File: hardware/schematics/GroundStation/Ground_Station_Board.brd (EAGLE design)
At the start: 50.5 x 66 mm, 11 parts

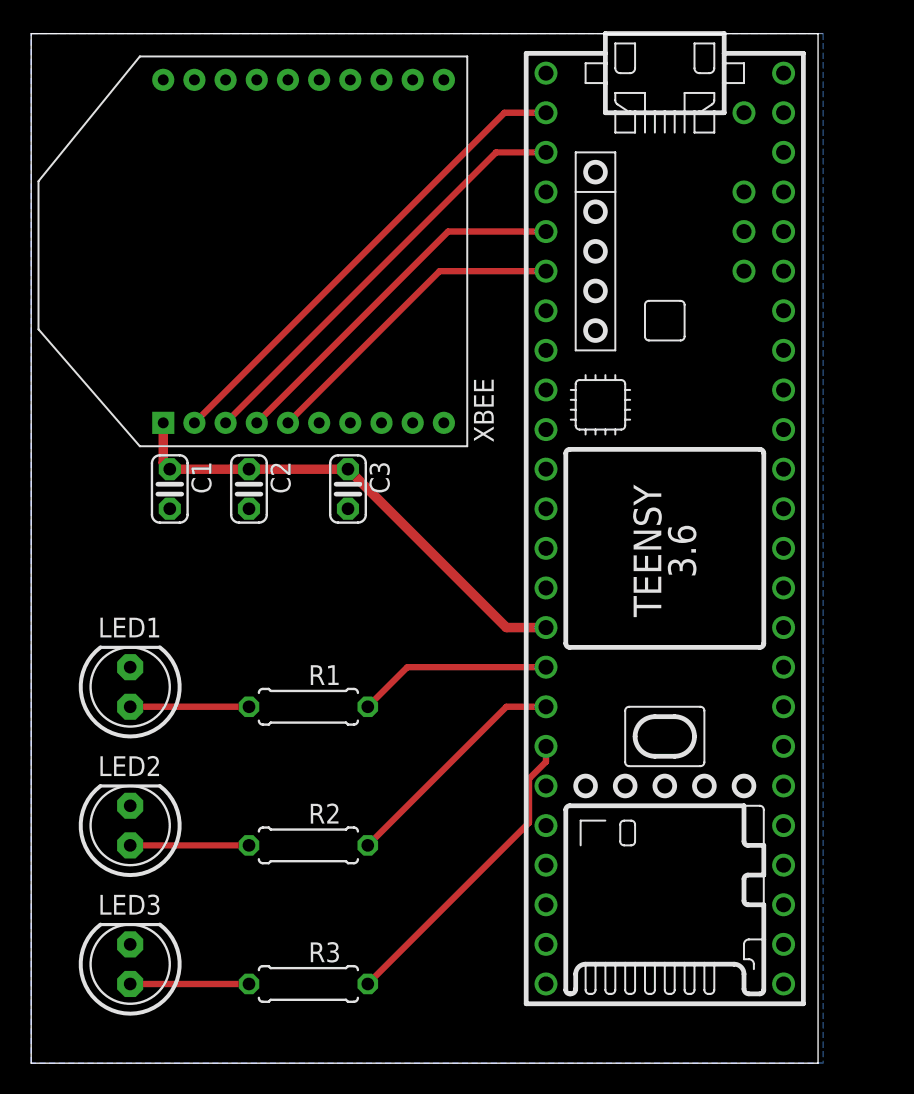
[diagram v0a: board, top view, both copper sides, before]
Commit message: Changed Xbee -> Xbee-Pro | Added render png
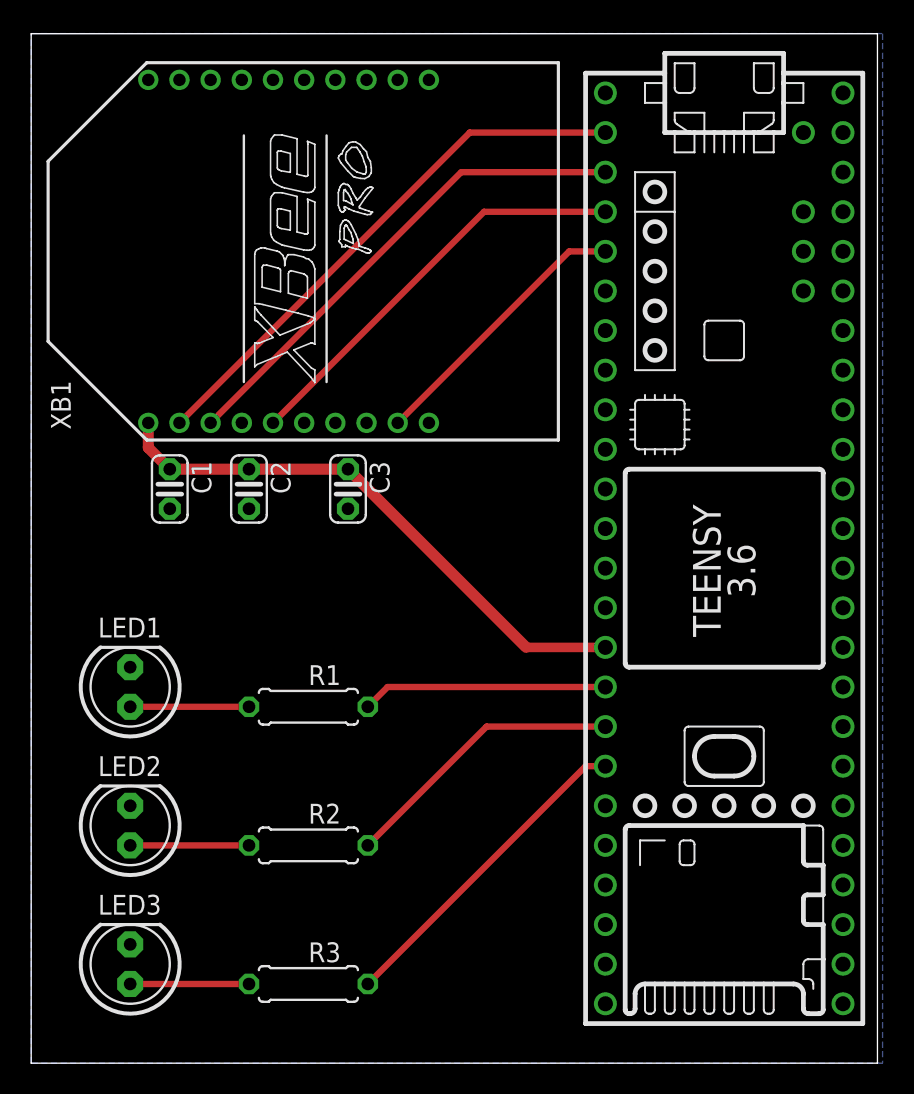
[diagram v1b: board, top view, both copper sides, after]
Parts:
- removed XBEE: XBEE, adafruit:XBEE
- added XB1: XBEE-PRO, xbee:XBEE-PRO
- moved U$2 4.02 mm to (44.5, 48.3)
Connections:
- net +3V3: now also XB1.1; no longer XBEE.1
- net GND: now also XB1.10, XB1.14; no longer XBEE.10, XBEE.14
- net XBEE_EN: now also XB1.9; no longer XBEE.4
- net XBEE_RST: now also U$2.2, XB1.5; no longer U$2.4/CANRX, XBEE.5
- net XBEE_RX: now also XB1.3; no longer XBEE.3
- net XBEE_TX: now also XB1.2; no longer XBEE.2
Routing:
- net XBEE_RST: track 20.6 -> 26.9 mm
- net XBEE_EN: track 23.6 -> 17.9 mm
- net +3V3: track 31.5 -> 36.8 mm
- net XBEE_RX: track 27.7 -> 32.0 mm
- net XBEE_TX: track 30.8 -> 35.0 mm
- net LED_2: track 15.1 -> 18.4 mm
- net LED_1: track 12.5 -> 15.8 mm
- net LED_3: track 20.0 -> 21.0 mm
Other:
- board size 50.5 x 66 mm -> 54.3 x 66 mm
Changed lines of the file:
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@@
 <drawing>
 <settings>
-<setting alwaysvectorfont="no"/>
+<setting alwaysvectorfont="yes"/>
 <setting verticaltext="up"/>
 </settings>
@@
 <layers>
 <layer number="1" name="Top" color="4" fill="1" visible="yes" active="yes"/>
+<layer number="2" name="Route2" color="1" fill="3" visible="no" active="no"/>
+<layer number="3" name="Route3" color="4" fill="3" visible="no" active="no"/>
+<layer number="4" name="Route4" color="1" fill="4" visible="no" active="no"/>
+<layer number="5" name="Route5" color="4" fill="4" visible="no" active="no"/>
+<layer number="6" name="Route6" color="1" fill="8" visible="no" active="no"/>
+<layer number="7" name="Route7" color="4" fill="8" visible="no" active="no"/>
+<layer number="8" name="Route8" color="1" fill="2" visible="no" active="no"/>
+<layer number="9" name="Route9" color="4" fill="2" visible="no" active="no"/>
+<layer number="10" name="Route10" color="1" fill="7" visible="no" active="no"/>
+<layer number="11" name="Route11" color="4" fill="7" visible="no" active="no"/>
+<layer number="12" name="Route12" color="1" fill="5" visible="no" active="no"/>
+<layer number="13" name="Route13" color="4" fill="5" visible="no" active="no"/>
+<layer number="14" name="Route14" color="1" fill="6" visible="no" active="no"/>
+<layer number="15" name="Route15" color="4" fill="6" visible="no" active="no"/>
 <layer number="16" name="Bottom" color="1" fill="1" visible="yes" active="yes"/>
 <layer number="17" name="Pads" color="2" fill="1" visible="yes" active="yes"/>
@@
 <board>
 <plain>
-<wire x1="0" y1="13.97" x2="50.47" y2="13.97" width="0" layer="20"/>
-<wire x1="50.47" y1="13.97" x2="50.47" y2="80" width="0" layer="20"/>
-<wire x1="50.47" y1="80" x2="0" y2="80" width="0" layer="20"/>
+<wire x1="0" y1="13.97" x2="54.28" y2="13.97" width="0" layer="20"/>
+<wire x1="54.28" y1="13.97" x2="54.28" y2="80" width="0" layer="20"/>
+<wire x1="54.28" y1="80" x2="0" y2="80" width="0" layer="20"/>
 <wire x1="0" y1="80" x2="0" y2="13.97" width="0" layer="20"/>
 </plain>
@@
 <attribute name="VALUE" x="18.034" y="18.4912" size="1.27" layer="27" ratio="10"/>
 </element>
-<element name="XBEE" library="adafruit" library_urn="urn:adsk.eagle:library:420" package="XBEE" package3d_urn="urn:adsk.eagle:package:6240840/1" value="XBEE" x="13.97" y="66.04" smashed="yes" rot="R90">
-<attribute name="NAME" x="28.4" y="57.91" size="1.27" layer="25" rot="R270"/>
-</element>
-<element name="U$2" library="Teensy356" package="TEENSY_3.5/3.6_BASIC" value="TEENSY_3.5/3.6_BASIC" x="40.64" y="49.53" smashed="yes" rot="R270"/>
+<element name="U$2" library="Teensy356" package="TEENSY_3.5/3.6_BASIC" value="TEENSY_3.5/3.6_BASIC" x="44.45" y="48.26" smashed="yes" rot="R270"/>
+<element name="XB1" library="xbee" package="XBEE-PRO" value="XBEE-PRO" x="16.51" y="66.04" smashed="yes" rot="R90">
+<attribute name="MF" value="" x="16.51" y="66.04" size="1.778" layer="27" rot="R90" display="off"/>
+<attribute name="MPN" value="XBP24-AWI-001" x="16.51" y="66.04" size="1.778" layer="27" rot="R90" display="off"/>
+<attribute name="NAME" x="2.54" y="54.61" size="1.27" layer="25" rot="R90"/>
+<attribute name="OC_FARNELL" value="1337916" x="16.51" y="66.04" size="1.778" layer="27" rot="R90" display="off"/>
+<attribute name="OC_NEWARK" value="42M2667" x="16.51" y="66.04" size="1.778" layer="27" rot="R90" display="off"/>
+<attribute name="VALUE" x="35.81" y="54.61" size="1.27" layer="27" rot="R90"/>
+</element>
 </elements>
 <signals>
 <signal name="GND">
-<contactref element="XBEE" pad="10"/>
-<contactref element="XBEE" pad="14"/>
 <contactref element="C2" pad="2"/>
 <contactref element="C1" pad="2"/>
@@
 <polygon width="0.1524" layer="16">
 <vertex x="0" y="80.01"/>
-<vertex x="50.8" y="80.01"/>
-<vertex x="50.8" y="13.97"/>
+<vertex x="54.61" y="80.01"/>
+<vertex x="54.61" y="13.97"/>
 <vertex x="0" y="13.97"/>
 </polygon>
+<contactref element="XB1" pad="10"/>
+<contactref element="XB1" pad="14"/>
 </signal>
 <signal name="XBEE_TX">
-<contactref element="XBEE" pad="2"/>
 <contactref element="U$2" pad="0/RX"/>
-<wire x1="10.47" y1="55.04" x2="30.36" y2="74.93" width="0.4064" layer="1"/>
-<wire x1="30.36" y1="74.93" x2="33.02" y2="74.93" width="0.4064" layer="1"/>
+<contactref element="XB1" pad="2"/>
+<wire x1="9.51" y1="55.04" x2="28.13" y2="73.66" width="0.4064" layer="1"/>
+<wire x1="28.13" y1="73.66" x2="36.83" y2="73.66" width="0.4064" layer="1"/>
 </signal>
 <signal name="XBEE_RX">
-<contactref element="XBEE" pad="3"/>
 <contactref element="U$2" pad="1/TX"/>
-<wire x1="12.47" y1="55.04" x2="29.82" y2="72.39" width="0.4064" layer="1"/>
-<wire x1="29.82" y1="72.39" x2="33.02" y2="72.39" width="0.4064" layer="1"/>
+<contactref element="XB1" pad="3"/>
+<wire x1="11.51" y1="55.04" x2="27.59" y2="71.12" width="0.4064" layer="1"/>
+<wire x1="27.59" y1="71.12" x2="36.83" y2="71.12" width="0.4064" layer="1"/>
 </signal>
 <signal name="XBEE_EN">
-<contactref element="XBEE" pad="4"/>
+<contactref element="XB1" pad="9"/>
 <contactref element="U$2" pad="3/CANTX"/>
-<wire x1="14.47" y1="55.04" x2="26.74" y2="67.31" width="0.4064" layer="1"/>
-<wire x1="26.74" y1="67.31" x2="33.02" y2="67.31" width="0.4064" layer="1"/>
+<wire x1="23.51" y1="55.04" x2="34.51" y2="66.04" width="0.4064" layer="1"/>
+<wire x1="34.51" y1="66.04" x2="36.83" y2="66.04" width="0.4064" layer="1"/>
 </signal>
 <signal name="XBEE_RST">
-<contactref element="XBEE" pad="5"/>
-<contactref element="U$2" pad="4/CANRX"/>
-<wire x1="16.47" y1="55.04" x2="26.2" y2="64.77" width="0.4064" layer="1"/>
-<wire x1="26.2" y1="64.77" x2="33.02" y2="64.77" width="0.4064" layer="1"/>
+<contactref element="XB1" pad="5"/>
+<contactref element="U$2" pad="2"/>
+<wire x1="29.05" y1="68.58" x2="36.83" y2="68.58" width="0.4064" layer="1"/>
+<wire x1="15.51" y1="55.04" x2="29.05" y2="68.58" width="0.4064" layer="1"/>
 </signal>
 <signal name="V_USB">
@@
 </signal>
 <signal name="+3V3">
-<contactref element="XBEE" pad="1"/>
 <contactref element="C2" pad="1"/>
 <contactref element="C3" pad="1"/>
 <contactref element="C1" pad="1"/>
-<wire x1="8.47" y1="55.04" x2="8.47" y2="52.49" width="0.6096" layer="1"/>
 <wire x1="8.89" y1="52.07" x2="8.47" y2="52.49" width="0.6096" layer="1"/>
-<wire x1="13.97" y1="52.07" x2="8.89" y2="52.07" width="0.6096" layer="1"/>
-<wire x1="13.97" y1="52.07" x2="20.32" y2="52.07" width="0.6096" layer="1"/>
+<wire x1="13.97" y1="52.07" x2="8.89" y2="52.07" width="0.7112" layer="1"/>
+<wire x1="13.97" y1="52.07" x2="20.32" y2="52.07" width="0.7112" layer="1"/>
 <contactref element="U$2" pad="3V3"/>
-<wire x1="20.32" y1="52.07" x2="30.48" y2="41.91" width="0.6096" layer="1"/>
-<wire x1="30.48" y1="41.91" x2="33.02" y2="41.91" width="0.6096" layer="1"/>
+<wire x1="20.32" y1="52.07" x2="31.75" y2="40.64" width="0.7112" layer="1"/>
+<wire x1="31.75" y1="40.64" x2="36.83" y2="40.64" width="0.6096" layer="1"/>
+<contactref element="XB1" pad="1"/>
+<wire x1="8.89" y1="52.07" x2="7.51" y2="53.45" width="0.7112" layer="1"/>
+<wire x1="7.51" y1="53.45" x2="7.51" y2="55.04" width="0.7112" layer="1"/>
 </signal>
 <signal name="LED_1">
 <contactref element="R1" pad="2"/>
 <contactref element="U$2" pad="24"/>
-<wire x1="21.59" y1="36.83" x2="24.13" y2="39.37" width="0.4064" layer="1"/>
-<wire x1="24.13" y1="39.37" x2="33.02" y2="39.37" width="0.4064" layer="1"/>
+<wire x1="21.59" y1="36.83" x2="22.86" y2="38.1" width="0.4064" layer="1"/>
+<wire x1="22.86" y1="38.1" x2="36.83" y2="38.1" width="0.4064" layer="1"/>
 </signal>
 <signal name="LED_2">
 <contactref element="R2" pad="2"/>
 <contactref element="U$2" pad="25"/>
-<wire x1="21.59" y1="27.94" x2="30.48" y2="36.83" width="0.4064" layer="1"/>
-<wire x1="30.48" y1="36.83" x2="33.02" y2="36.83" width="0.4064" layer="1"/>
+<wire x1="21.59" y1="27.94" x2="29.21" y2="35.56" width="0.4064" layer="1"/>
+<wire x1="29.21" y1="35.56" x2="36.83" y2="35.56" width="0.4064" layer="1"/>
 </signal>
 <signal name="LED_3">
 <contactref element="R3" pad="2"/>
 <contactref element="U$2" pad="26"/>
-<wire x1="21.59" y1="19.05" x2="31.9278" y2="29.3878" width="0.4064" layer="1"/>
-<wire x1="33.02" y1="33.29460625" x2="33.02" y2="34.29" width="0.4064" layer="1"/>
-<wire x1="31.9278" y1="32.20240625" x2="33.02" y2="33.29460625" width="0.4064" layer="1"/>
-<wire x1="31.9278" y1="29.3878" x2="31.9278" y2="32.20240625" width="0.4064" layer="1"/>
+<wire x1="21.59" y1="19.05" x2="35.56" y2="33.02" width="0.4064" layer="1"/>
+<wire x1="35.56" y1="33.02" x2="36.83" y2="33.02" width="0.4064" layer="1"/>
 </signal>
 <signal name="N$1">
@@
 </signals>
 <mfgpreviewcolors>
-<mfgpreviewcolor name="soldermaskcolor" color="0xC8008000"/>
+<mfgpreviewcolor name="soldermaskcolor" color="0xC8000000"/>
 <mfgpreviewcolor name="silkscreencolor" color="0xFFFEFEFE"/>
 <mfgpreviewcolor name="backgroundcolor" color="0xFF282828"/>
